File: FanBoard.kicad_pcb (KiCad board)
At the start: 2 copper layers, 45.1 x 33 mm, 21 parts, among them Q1 BUK9M34-100EX, Q2 BUK9M34-100EX, Q3 BUK9M34-100EX, Q4 BUK9M34-100EX

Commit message: Updates reference
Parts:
- removed G***: LOGO, UTSVT_Special:Hallock_Image_Small
- removed G***: LOGO, UTSVT_Special:UTSVT_Logo_Symbol
- D1, D2, D3, D4: footprint UTSVT_BPS:V2F22HM -> UTSVT_Passive:V2F22HM
- LED1: renamed from STATUS; value LED -> STATUS
- renumbered LDRBRDConn to J1, FAN1 to J2, FAN2 to J3, FAN3 to J4, FAN4 to J5
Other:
- board text added: "UTSVT - BPS Fan Board v1.0 Summer 2020"
- board text removed: "UTSVT - BPS Fan Board v2.0 Summer 2020"

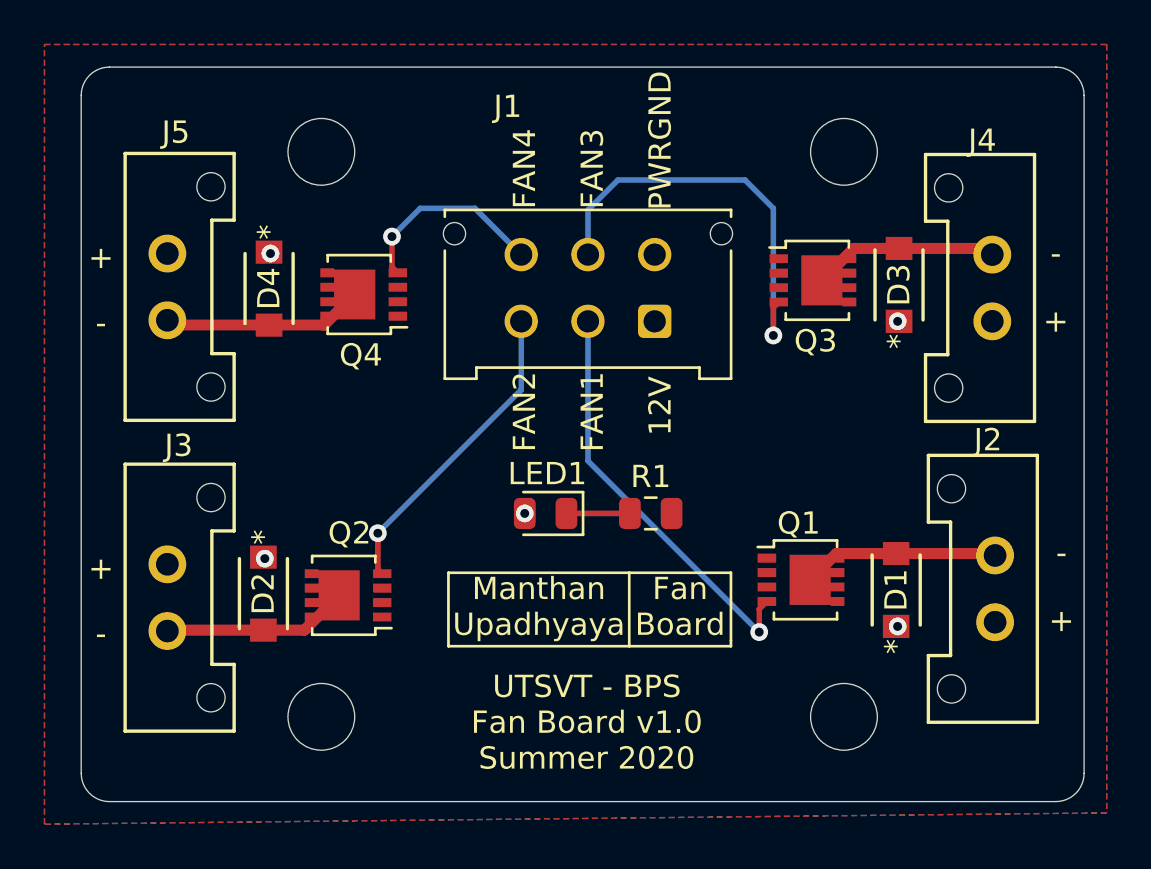
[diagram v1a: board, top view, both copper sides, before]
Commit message: Changed symbol and footprint library paths to include new repositories. Fixed issues with graphic footprints and reference labels
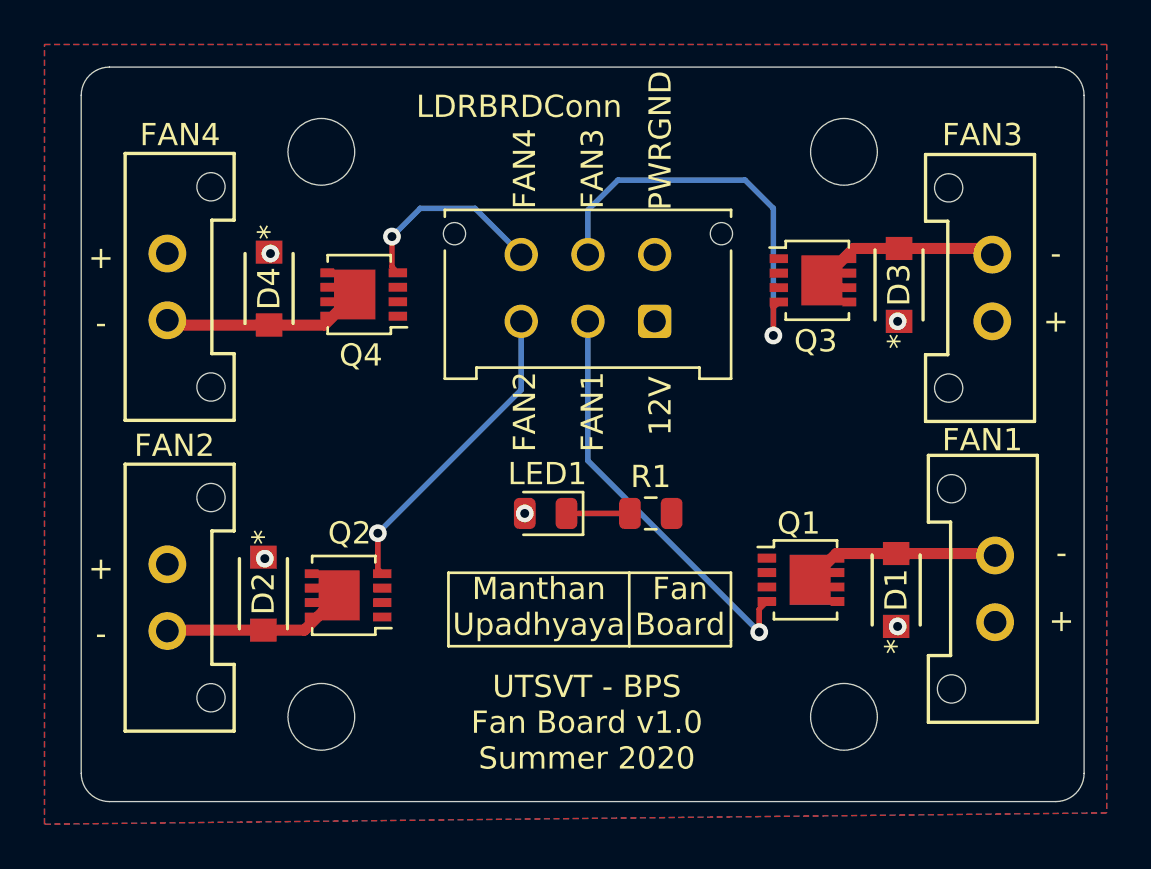
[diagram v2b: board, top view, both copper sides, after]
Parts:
- added LOGO1: Hallock, UTSVT_Special:Hallock_Image_Small, B.Cu at (161.3, 68.1)
- added LOGO2: UTSVT, UTSVT_Special:UTSVT_Logo_Symbol, B.Cu at (148.1, 69.3)
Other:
- board text added: "LDRBRDConn"

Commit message: Fixed resistor value and created Gerber files
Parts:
- R1: value 45k -> 5.05k
